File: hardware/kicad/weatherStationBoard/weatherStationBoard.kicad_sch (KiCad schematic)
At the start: 29 parts, among them J1 USB_C_Receptacle_USB2.0_16P, Q1 S8050, Q2 S8050, U1 ESP-12F, U2 CH340G, U4 AMS1117-3.3, Y1 Crystal_GND24_Small

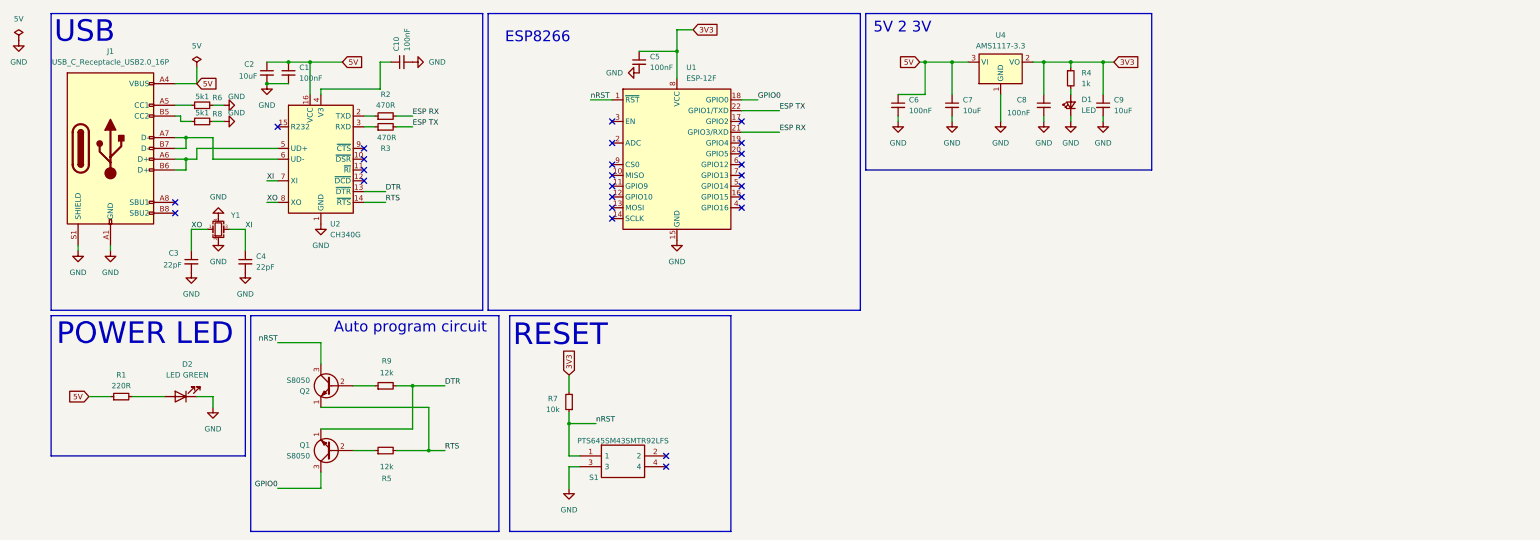
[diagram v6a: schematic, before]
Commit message: Added BME680 Display-Connector and Mounting holes - 3D model of USB connector and Readme assets
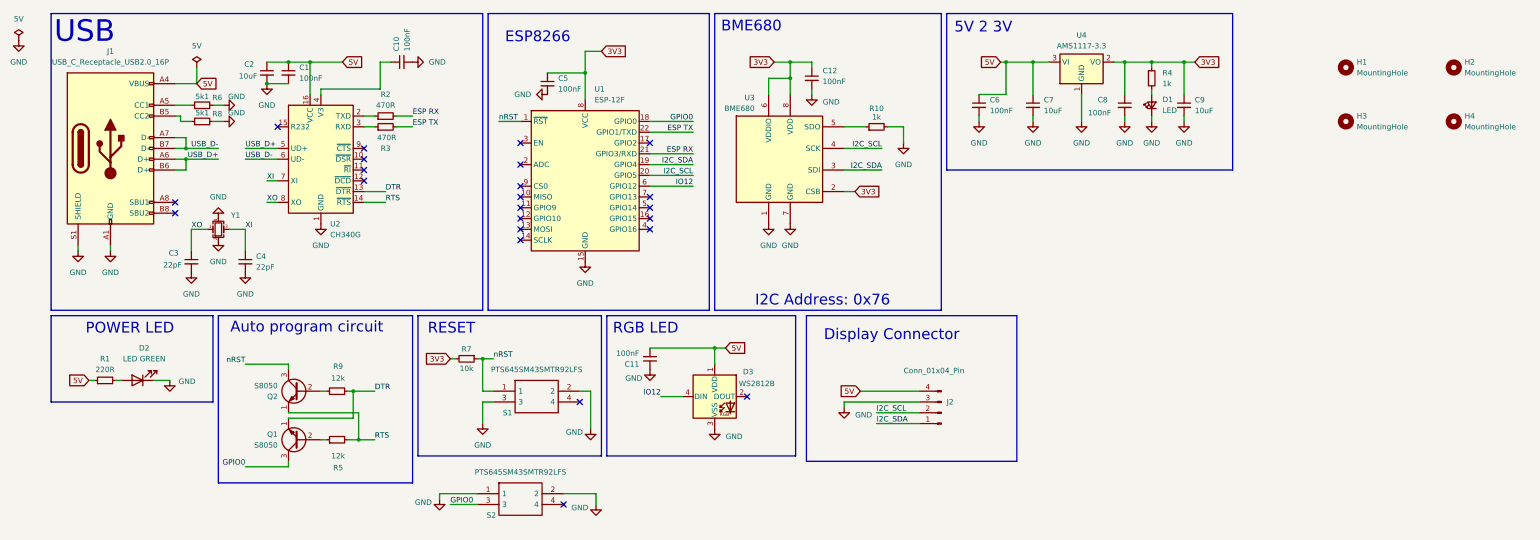
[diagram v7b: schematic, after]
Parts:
- added C11, C12: 100nF, Capacitor_SMD:C_0805_2012Metric, symbol Device:C_Small
- added D3: WS2812B, LED_SMD:LED_WS2812B_PLCC4_5.0x5.0mm_P3.2mm, symbol LED:WS2812B
- added H1, H2, H3, H4: MountingHole, MountingHole:MountingHole_2.5mm, symbol Mechanical:MountingHole
- added J2: Conn_01x04_Pin, Connector_JST:JST_PH_B4B-PH-K_1x04_P2.00mm_Vertical, symbol Connector:Conn_01x04_Pin
- added R10: 1k, Resistor_SMD:R_0805_2012Metric, symbol Device:R_Small
- added S2: PTS645SM43SMTR92LFS, PTS645SM43SMTR92LFS:PTS645_SMT_, symbol PTS645SM43SMTR92LFS:PTS645SM43SMTR92LFS
- added U3: BME680, Package_LGA:Bosch_LGA-8_3x3mm_P0.8mm_ClockwisePinNumbering, symbol Sensor:BME680
- J1: footprint Connector_USB:USB_C_Receptacle_XKB_U262-16XN-4BVC11 -> Connector_USB:USB_C_Receptacle_HRO_TYPE-C-31-M-12
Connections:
- net 3V3: now also C12.1, U3.2 (CSB), U3.6 (VDDIO), U3.8 (VDD)
- net 5V: now also C11.2, D3.1 (VDD), J2.4 (Pin_4)
- net GND: now also S1.2, C11.1, C12.2, D3.3 (VSS), J2.3 (Pin_3), R10.2, S2.1, S2.2, U3.1 (GND), U3.7 (GND)
- net GPIO0: now also S2.3
- net I2C_SDA: now reaches U1.19 (GPIO4)
- net I2C_SDA: now also J2.1 (Pin_1), U3.3 (SDI)
- net I2C_SCL: now reaches U1.20 (GPIO5)
- net I2C_SCL: now also J2.2 (Pin_2), U3.4 (SCK)
- net IO12: now reaches U1.6 (GPIO12)
- net IO12: now also D3.4 (DIN)
- net USB_D+: now reaches J1.A6 (D+), J1.B6 (D+), U2.5 (UD+)
- net USB_D-: now reaches J1.A7 (D-), J1.B7 (D-), U2.6 (UD-)
- new net: R10.1, U3.5 (SDO)
- no-connect marks 25 -> 23
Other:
- note added: "BME680"
- note added: "Display Connector"
- note added: "I2C Address: 0x76"
- note added: "RGB LED"
- moved on the sheet: C5, C6, C7, C8, C9, D1, D2, Q1, Q2, R1, R4, R5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

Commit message: Board&Case
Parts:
- removed J2: Conn_01x04_Pin, Connector_JST:JST_PH_B4B-PH-K_1x04_P2.00mm_Vertical, symbol Connector:Conn_01x04_Pin
- added C13, C15: 1uF, Capacitor_SMD:C_0805_2012Metric, symbol Device:C_Polarized_Small
- added C14: 10uF, Capacitor_SMD:C_0805_2012Metric, symbol Device:C_Small
- added C16: 1uF, Capacitor_SMD:C_0805_2012Metric, symbol Device:C_Small
- added C17: 2uF, Capacitor_SMD:C_0805_2012Metric, symbol Device:C_Small
- added C18: 100nF, Capacitor_SMD:C_0805_2012Metric, symbol Device:C_Small
- added D4: 1N4148W, Diode_SMD:D_SOD-123, symbol Diode:1N4148W
- added J3: Conn_01x30_Pin, SSD1306:SSD1306_ribbon, symbol Connector:Conn_01x30_Pin
- added R11: 1k, Resistor_SMD:R_0805_2012Metric, symbol Device:R_Small
- added R12, R13: 10k, Resistor_SMD:R_0805_2012Metric, symbol Device:R_Small
- added R14: 390K, Resistor_SMD:R_0805_2012Metric, symbol Device:R_Small
- H1, H2, H3, H4: footprint MountingHole:MountingHole_2.5mm -> MountingHole:MountingHole_2.2mm_M2
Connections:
- net 3V3: now also D4.1 (K), J3.11 (Pin_11), J3.6 (Pin_6), J3.9 (Pin_9), R11.2, R12.1, R13.2
- net GND: now also C14.2, C16.2, C17.2, C18.2, J3.1 (Pin_1), J3.10 (Pin_10), J3.12 (Pin_12), J3.13 (Pin_13), J3.15 (Pin_15), J3.16 (Pin_16), J3.17 (Pin_17), J3.21 (Pin_21), J3.22 (Pin_22), J3.23 (Pin_23), J3.24 (Pin_24), J3.25 (Pin_25), J3.8 (Pin_8), R14.1
- net I2C_SCL: now also J3.18 (Pin_18), R12.2
- net I2C_SDA: now also J3.19 (Pin_19), J3.20 (Pin_20), R13.1
- new net: C14.1, D4.2 (A), J3.14 (Pin_14), R11.1
- new net: C17.1, C18.1, J3.28 (Pin_28)
- new net: C15.1, J3.2 (Pin_2)
- new net: J3.26 (Pin_26), R14.2
- new net: C16.1, J3.27 (Pin_27)
- new net: J3.29 (Pin_29), J3.30 (Pin_30)
- new net: C15.2, J3.3 (Pin_3)
- new net: C13.1, J3.4 (Pin_4)
- new net: C13.2, J3.5 (Pin_5)
- no-connect marks 23 -> 24
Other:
- note added: "SSD1306"
- note removed: "Display Connector"
